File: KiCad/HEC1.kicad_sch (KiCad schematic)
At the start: 37 parts, among them J1 Barrel_Jack_Switch, U35 74LS08, U37 74LS32, U41 74LS02

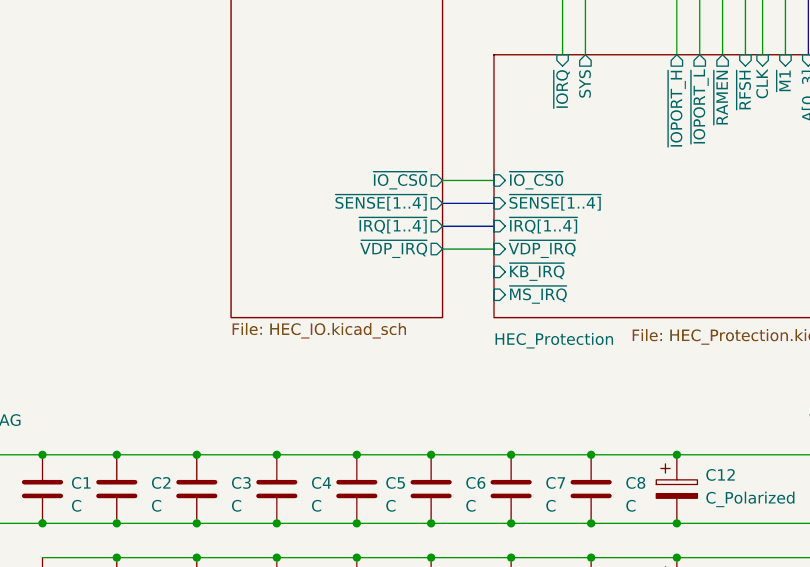
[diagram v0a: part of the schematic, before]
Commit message: Add keyboard circuit
Added symbol for HT6542B keyboard controller. Added keyboard and mouse support to IO circuit. Reduced ERC error to 0.
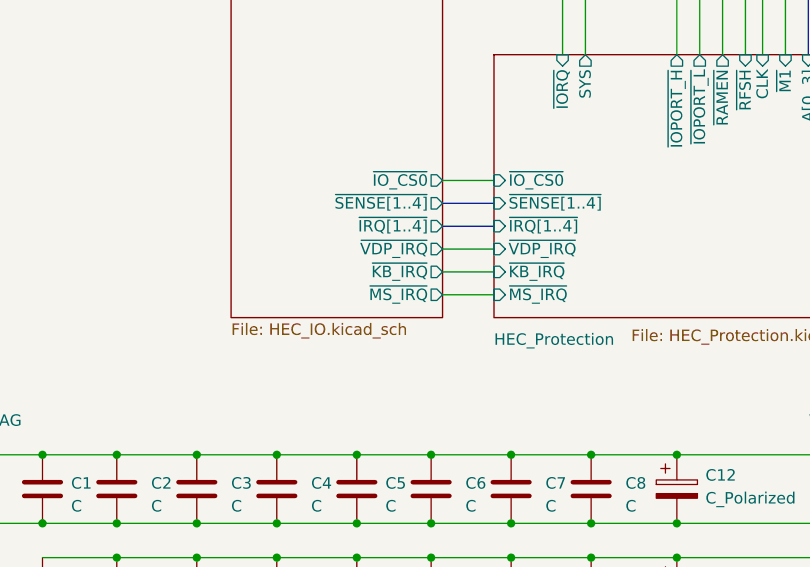
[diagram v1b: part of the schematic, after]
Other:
- sheet HEC_IO ports: added ~{KB_IRQ}, ~{MS_IRQ}; removed none
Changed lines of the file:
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@@
+    (stroke (width 0) (type default))
+  )
+  (wire (pts (xy 118.11 109.22) (xy 123.825 109.22))
     (stroke (width 0) (type default))
   )
@@
   )
   (bus (pts (xy 118.11 74.295) (xy 161.29 74.295))
+    (stroke (width 0) (type default))
+  )
+  (wire (pts (xy 118.11 111.76) (xy 123.825 111.76))
     (stroke (width 0) (type default))
   )
@@
       (effects (font (size 1.27 1.27)) (justify right))
     )
+    (pin "~{KB_IRQ}" output (at 118.11 109.22 0)
+      (effects (font (size 1.27 1.27)) (justify right))
+    )
+    (pin "~{MS_IRQ}" output (at 118.11 111.76 0)
+      (effects (font (size 1.27 1.27)) (justify right))
+    )

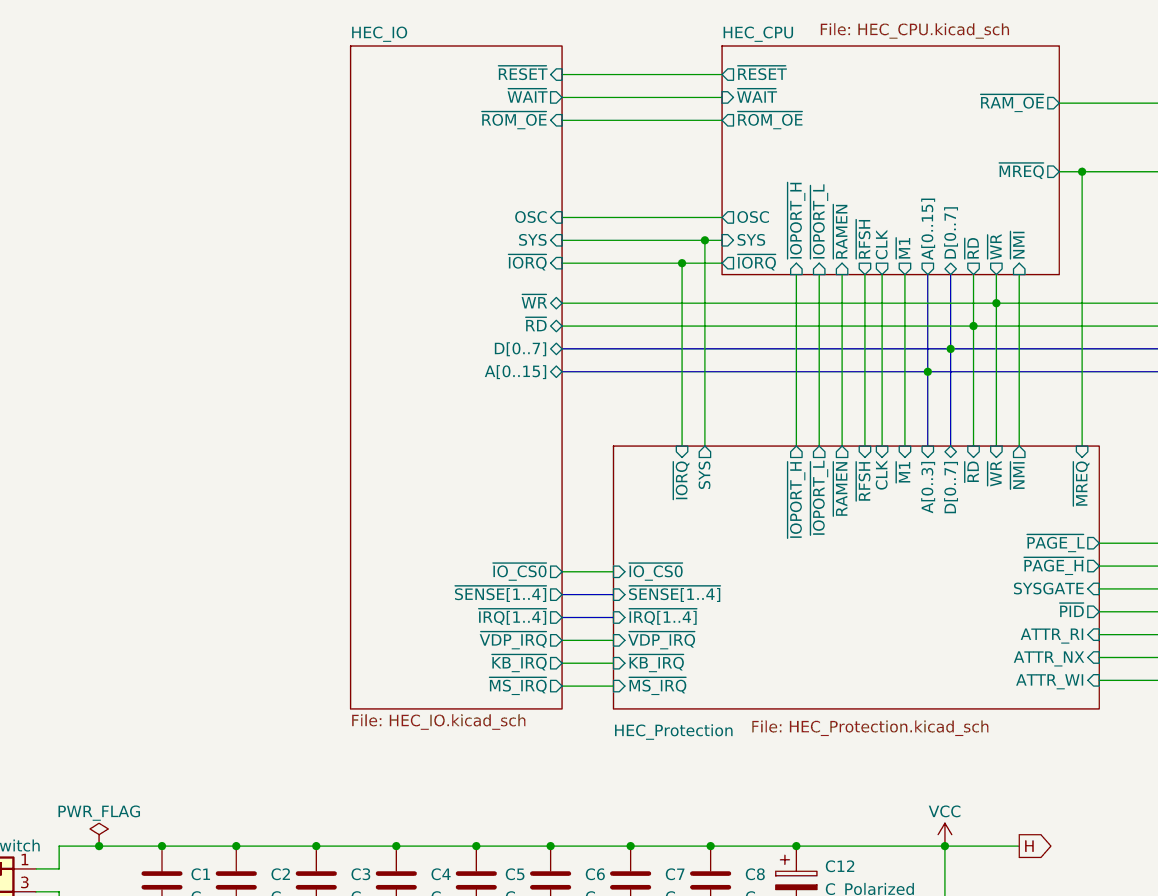
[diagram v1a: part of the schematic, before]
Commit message: Split peripherals into separate schematic
Split graphics/sound/storage (VERA) board connector and keyboard/mouse controller into a separate schematic file. Add joystick/controller port. This commit is seriously delayed by the controller port design, and it is still subject to change.
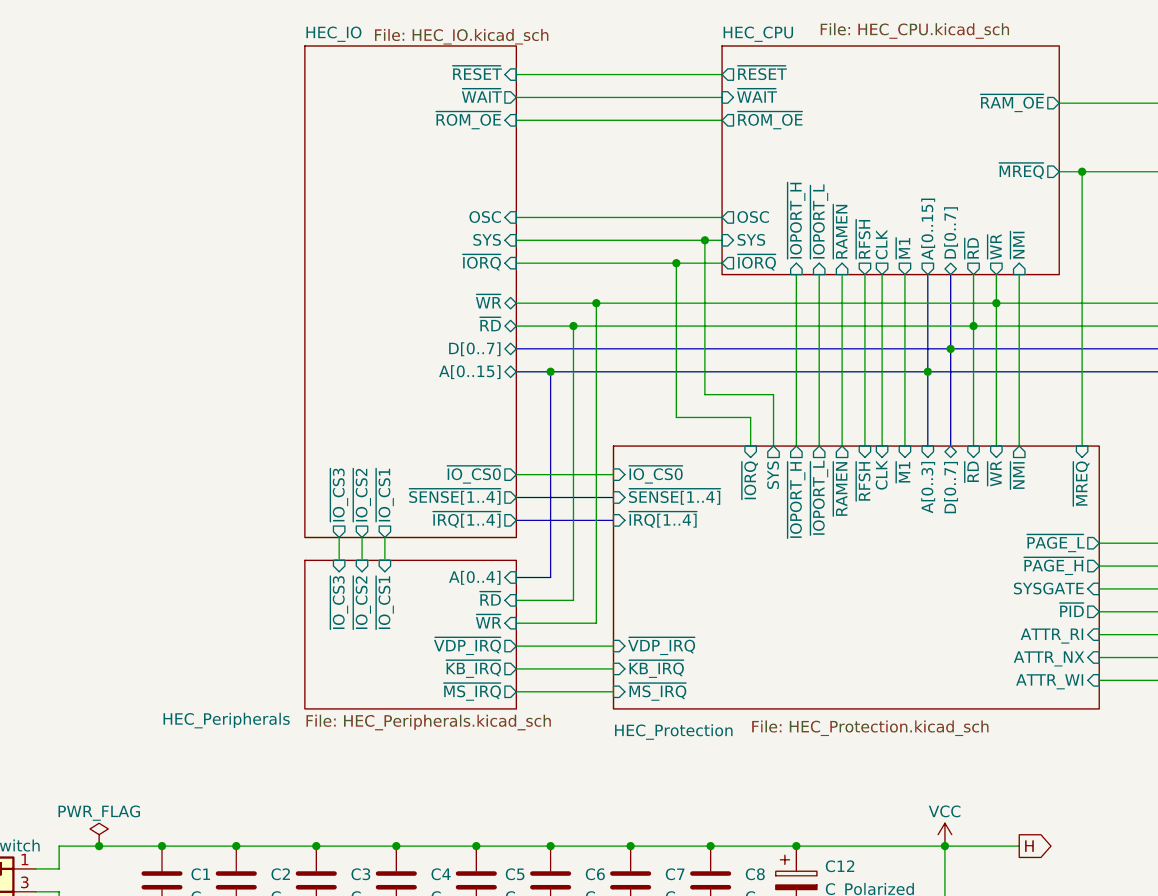
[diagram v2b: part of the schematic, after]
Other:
- added sheet HEC_Peripherals (HEC_Peripherals.kicad_sch)
- sheet HEC_IO ports: added ~{IO_CS1}, ~{IO_CS2}, ~{IO_CS3}; removed ~{KB_IRQ}, ~{MS_IRQ}, ~{VDP_IRQ}

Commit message: Add NES port
Added NES port from NES port breadboard project
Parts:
- U41: footprint (none) -> Package_DIP:DIP-14_W7.62mm_Socket
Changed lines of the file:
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@@
       (effects (font (size 1.27 1.27)))
     )
-    (property "Footprint" "" (at 207.645 150.495 0)
+    (property "Footprint" "Package_DIP:DIP-14_W7.62mm_Socket" (at 207.645 150.495 0)
       (effects (font (size 1.27 1.27)) hide)
     )
@@
       (effects (font (size 1.27 1.27)))
     )
-    (property "Footprint" "" (at 226.06 133.985 0)
+    (property "Footprint" "Package_DIP:DIP-14_W7.62mm_Socket" (at 226.06 133.985 0)
       (effects (font (size 1.27 1.27)) hide)
     )
@@
       (effects (font (size 1.27 1.27)))
     )
-    (property "Footprint" "" (at 227.965 150.495 0)
-      (effects (font (size 1.27 1.27)) hide)
-    )
+    (property "Footprint" "Package_DIP:DIP-14_W7.62mm_Socket" (at 227.965 150.495 0)
+      (effects (font (size 1.27 1.27)) hide)
+    )

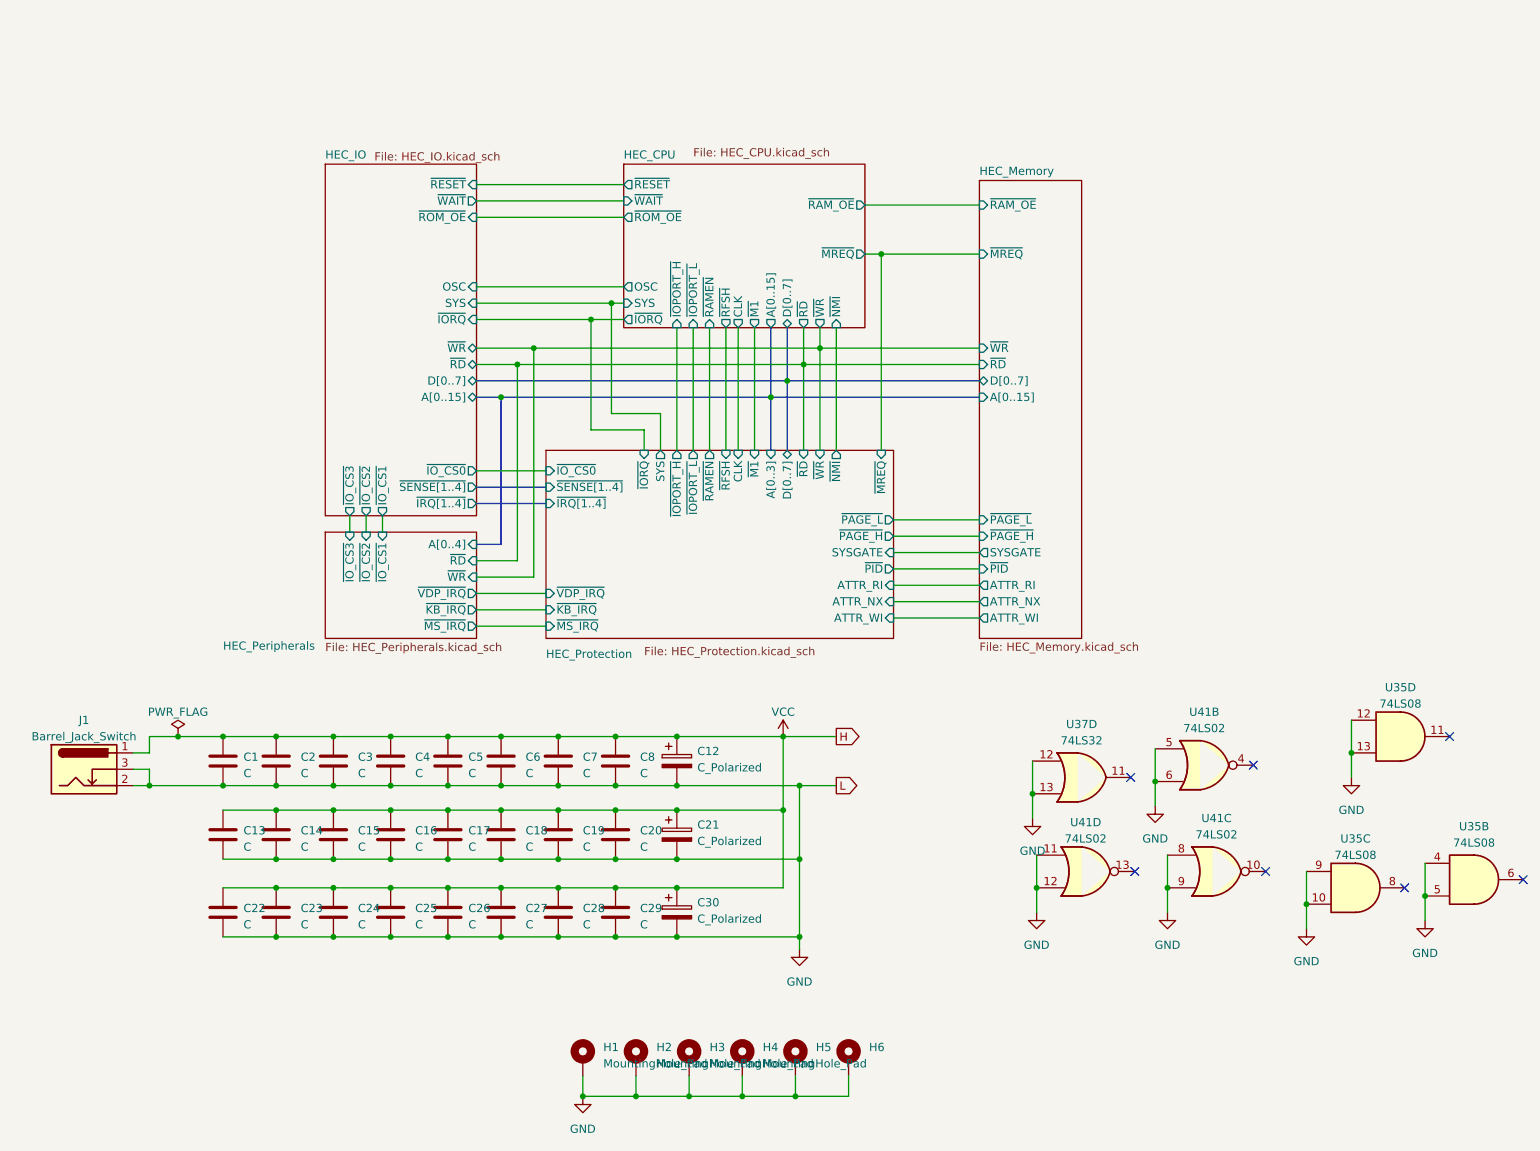
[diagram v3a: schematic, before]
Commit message: Removed DMA from bus
Bus-mastering DMA has been removed from the expansion bus design due to complexity and bandwidth issue with external bus expansion circuit. The pins are replaced with audio output from on-bard sound system. Minor changes to pin names.
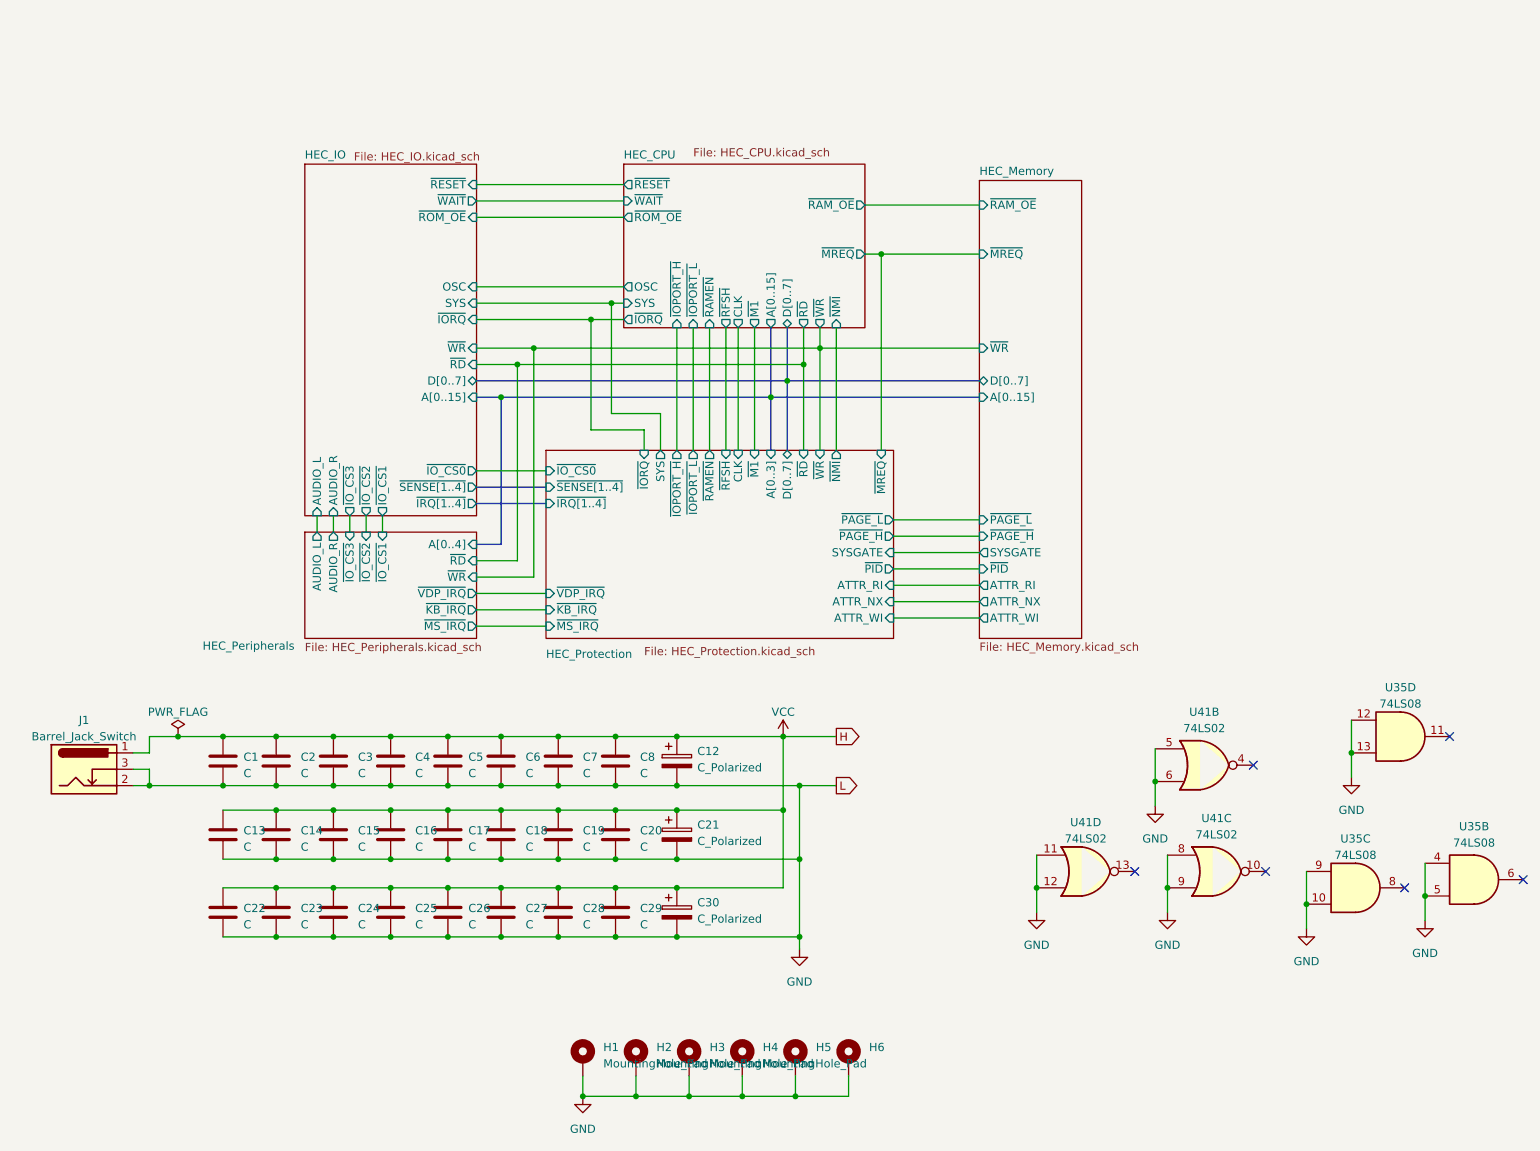
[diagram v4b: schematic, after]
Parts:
- removed U37: 74LS32, Package_DIP:DIP-14_W7.62mm_Socket, symbol 74xx:74LS32
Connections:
- no-connect marks 7 -> 6
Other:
- sheet HEC_IO ports: added AUDIO_L, AUDIO_R; removed none
- sheet HEC_Memory ports: added none; removed ~{RD}
- sheet HEC_Peripherals ports: added AUDIO_L, AUDIO_R; removed none
